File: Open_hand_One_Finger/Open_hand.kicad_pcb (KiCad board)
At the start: 2 copper layers, 21 x 101.6 mm, 28 parts, among them U1 LIS3MDL, U2 MAX32660GTP, U4 ICM-40608, U5 ICM-40608, U6 ICM-40608

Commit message: add swd conector
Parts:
- added C15: 1u, Capacitor_SMD:C_0603_1608Metric, F.Cu at (170.9, 108.7)
- added C16: 1u, Capacitor_SMD:C_0603_1608Metric, F.Cu at (170.9, 110.3)
- added C17: 1u, Capacitor_SMD:C_0603_1608Metric, F.Cu at (189.0, 106.4)
- added J1: Conn_ARM_JTAG_SWD_10, Connector:Tag-Connect_TC2050-IDC-FP_2x05_P1.27mm_Vertical, F.Cu at (184.0, 105.6)
- added Y1: 32.768kHz,6pF, Crystal:Crystal_SMD_3215-2Pin_3.2x1.5mm, F.Cu at (170.7, 105.9)
- moved U2 3.23 mm to (175.1, 107.6), turned to -90 degrees
- moved TP3 1.07 mm to (167.9, 102.9)
- moved TP2 0.76 mm to (165.5, 103.0)
- moved TP4 0.49 mm to (171.7, 102.6)
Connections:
- net /IMU/INT1 renamed /INT0
- net /IMU1/INT1 renamed /INT1
- net /IMU2/INT1 renamed /INT2
- net /MAG/DRDY renamed /DREADY
- U2 pad 10: unconnected-(U2-VCORE-Pad10) -> Net-(U2-VCORE)
- U2 pad 7: unconnected-(U2-32KOUT-Pad7) -> Net-(U2-32KOUT)
- U2 pad 8: unconnected-(U2-32KIN-Pad8) -> Net-(U2-32KIN)
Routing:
- net Net-(U2-32KOUT): track 0.00 -> 4.18 mm
- net Net-(U2-32KIN): track 0.00 -> 2.68 mm
- net Net-(U2-VCORE): track 0.00 -> 2.60 mm
- net +3.3V: track 13.7 -> 15.5 mm
- net GND: track 19.4 -> 20.8 mm, vias 0 -> 2
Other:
- board size 21 x 101.6 mm -> 28.9 x 100 mm
- board text added: "0.0800 mm / 0.0800 mm"
- board text added: "0.1100 mm"
- board text added: "0.2500 mm"
- board text added: "2"
- board text added: "20.9898 mm x 99.9950 mm"
- board text added: "BOARD CHARACTERISTICS"
- board text added: "Board Thickness:"
- board text added: "Board overall dimensions:"
- board text added: "Castellated pads:"
- board text added: "Copper Finish:"
- board text added: "Copper Layer Count:"
- board text added: "Edge card connectors:"
- board text added: "Impedance Control:"
- board text added: "Min hole diameter:"
- board text added: "Min track/spacing:"
- board text added: "No"
- board text added: "None"
- board text added: "Plated Board Edge:"
- board text added: "Yes"

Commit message: making the pcb look less like a dick
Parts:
- added J2: DF37C-24DP-0.4V(51), DF37C-24DP-0.4V(51):DF37C-24DP-0.4V(51), B.Cu at (169.1, 124.5)
- moved TP9 13.4 mm to (167.3, 43.2)
- moved C10 9.67 mm to (171.5, 38.8)
- moved C11 9.67 mm to (173.6, 43.4)
- moved C9 9.67 mm to (171.5, 40.4)
- moved U6 9.67 mm to (171.5, 43.2)
- moved TP8 4.88 mm to (168.1, 65.2)
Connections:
- U1 pad 7: /MAG/INT -> /INT_MAG
- U2 pad 5: unconnected-(U2-~{RSTN}-Pad5) -> /RST
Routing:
- net +3.3V: track 15.5 -> 135.7 mm
- net /CS2: track 0.00 -> 69.3 mm
- net /DIN: track 4.11 -> 69.9 mm
- net /CLK: track 4.26 -> 70.0 mm
- net /DOUT: track 4.70 -> 69.7 mm, vias 4 -> 2
- net /INT2: track 0.00 -> 57.3 mm, vias 0 -> 1
- net /CS1: track 0.00 -> 5.84 mm, vias 0 -> 2
- net GND: track 20.8 -> 16.9 mm, vias 2 -> 10
- net /INT1: track 0.00 -> 1.84 mm
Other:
- board size 28.9 x 100 mm -> 28.9 x 88.2 mm

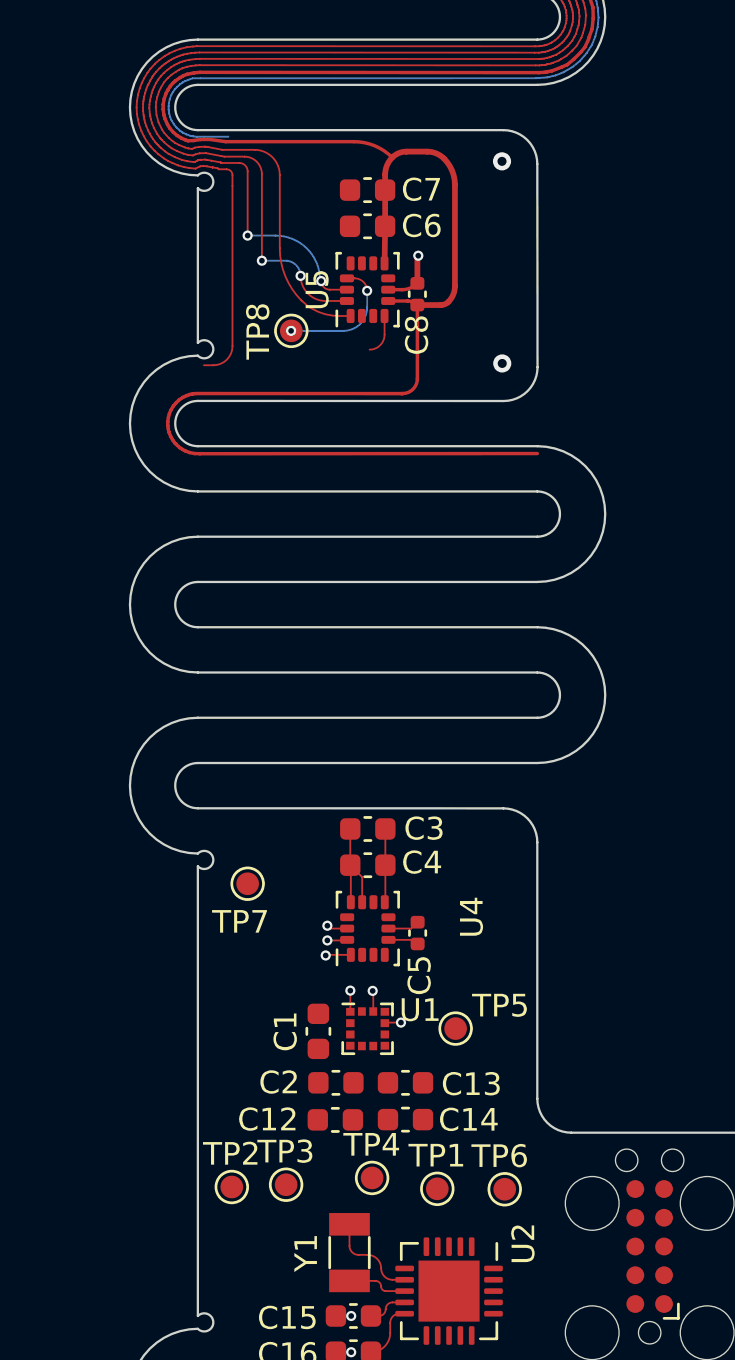
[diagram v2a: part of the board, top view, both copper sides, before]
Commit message: adding coverlay slit so emi shield is connected to gnd more routing
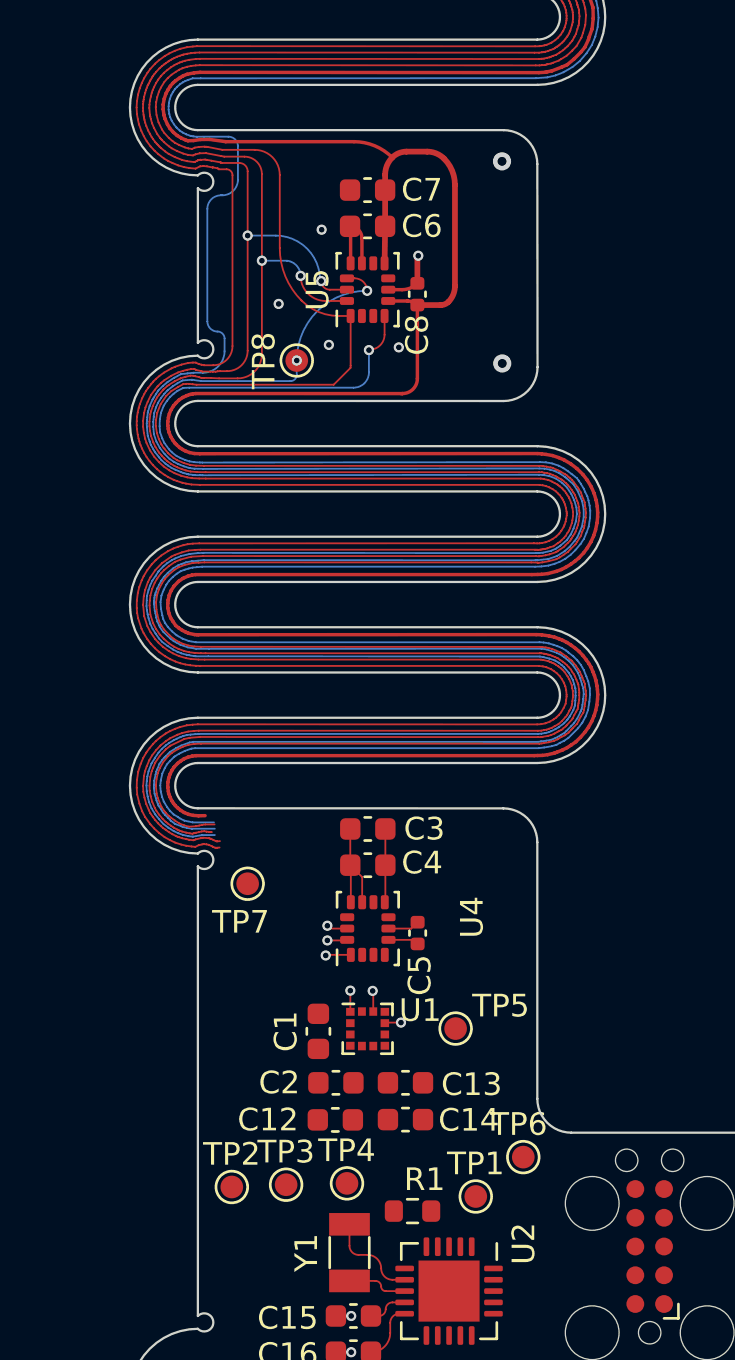
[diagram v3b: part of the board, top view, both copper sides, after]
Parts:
- added R1: R_US, Resistor_SMD:R_0603_1608Metric, F.Cu at (173.5, 104.1)
- moved TP1 1.73 mm to (176.3, 103.4)
- moved TP6 1.64 mm to (178.4, 101.7)
- moved TP8 1.33 mm to (168.4, 66.5)
- moved TP4 1.14 mm to (170.6, 102.8)
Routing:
- net /INT2: track 57.3 -> 162.9 mm
- net /CLK: track 70.0 -> 171.6 mm
- net /DOUT: track 69.7 -> 170.7 mm
- net /DIN: track 69.9 -> 169.9 mm
- net /INT1: track 1.84 -> 101.9 mm, vias 0 -> 1
- net /CS1: track 5.84 -> 103.1 mm
- net /CS2: track 69.3 -> 164.3 mm
- net +3.3V: track 135.7 -> 206.1 mm
- net GND: track 16.9 -> 20.4 mm, vias 10 -> 14

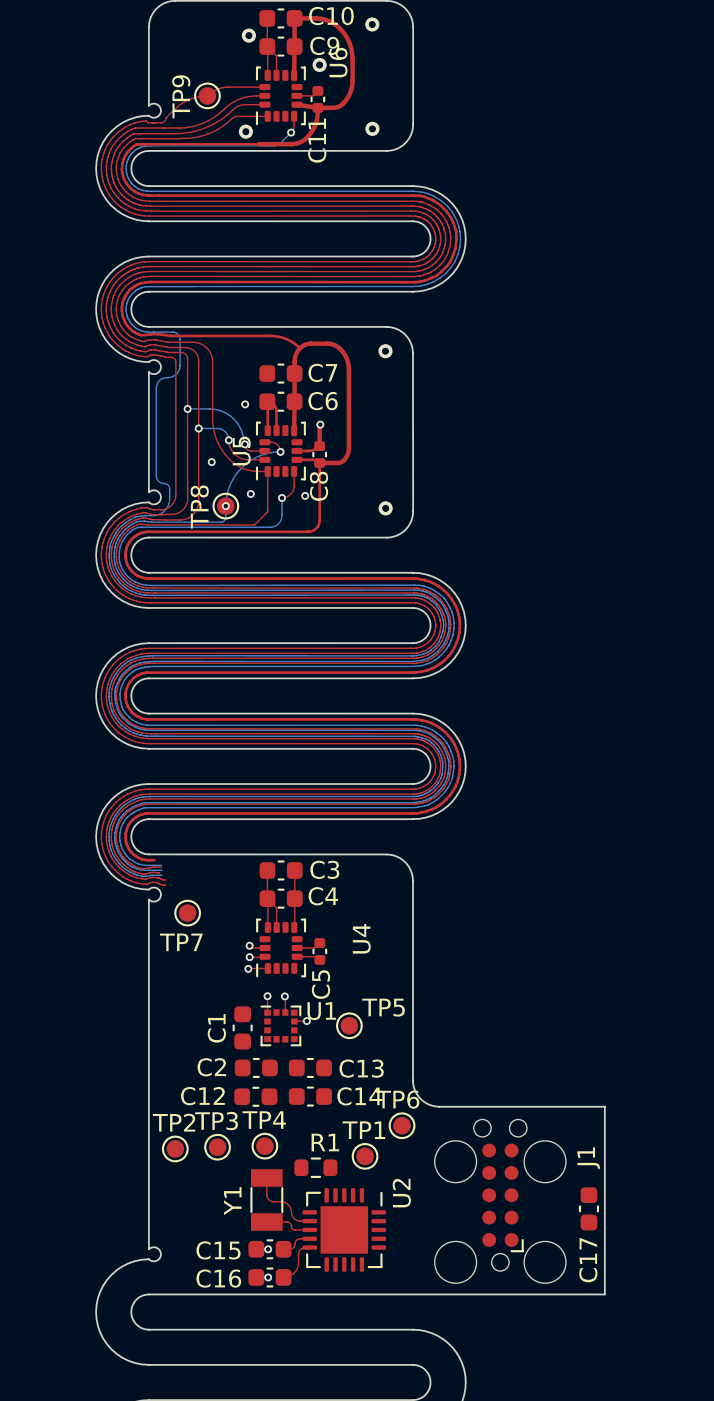
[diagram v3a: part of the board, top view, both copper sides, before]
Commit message: new copper pour rules
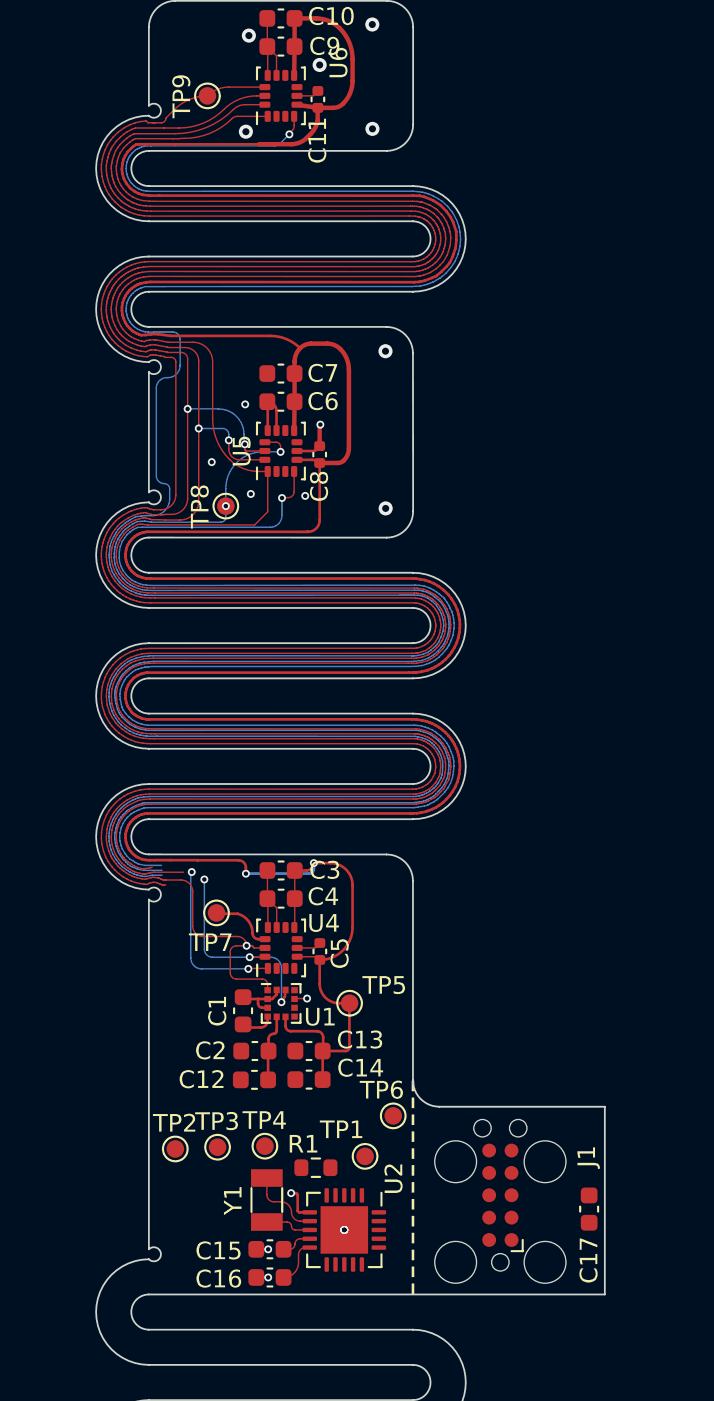
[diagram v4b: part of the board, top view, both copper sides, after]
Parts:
- moved TP7 1.64 mm to (167.8, 89.6)
- moved TP5 1.28 mm to (175.4, 94.7)
- moved U1 1.28 mm to (171.5, 94.7)
- moved C1 0.97 mm to (169.3, 95.2)
- moved C13 0.97 mm to (173.1, 97.4)
- moved C14 0.97 mm to (173.1, 99.1)
- moved C12 0.97 mm to (170.0, 99.1)
- moved C2 0.97 mm to (170.0, 97.4)
- moved TP6 0.75 mm to (177.9, 101.1)
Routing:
- net +3.3V: track 206.1 -> 242.9 mm, vias 0 -> 2
- net /CLK: track 171.6 -> 184.0 mm, vias 4 -> 3
- net /DIN: track 169.9 -> 182.3 mm, vias 4 -> 5
- net /DOUT: track 170.7 -> 178.7 mm, vias 2 -> 3
- net GND: track 20.4 -> 25.8 mm, vias 14 -> 18
- net /CS0: track 0.00 -> 3.59 mm
- net Net-(U1-C1): track 0.00 -> 1.92 mm
- net /CS1: track 103.1 -> 103.7 mm
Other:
- board text added: "28.8949 mm x 88.2250 mm"
- board text removed: "20.9898 mm x 99.9950 mm"

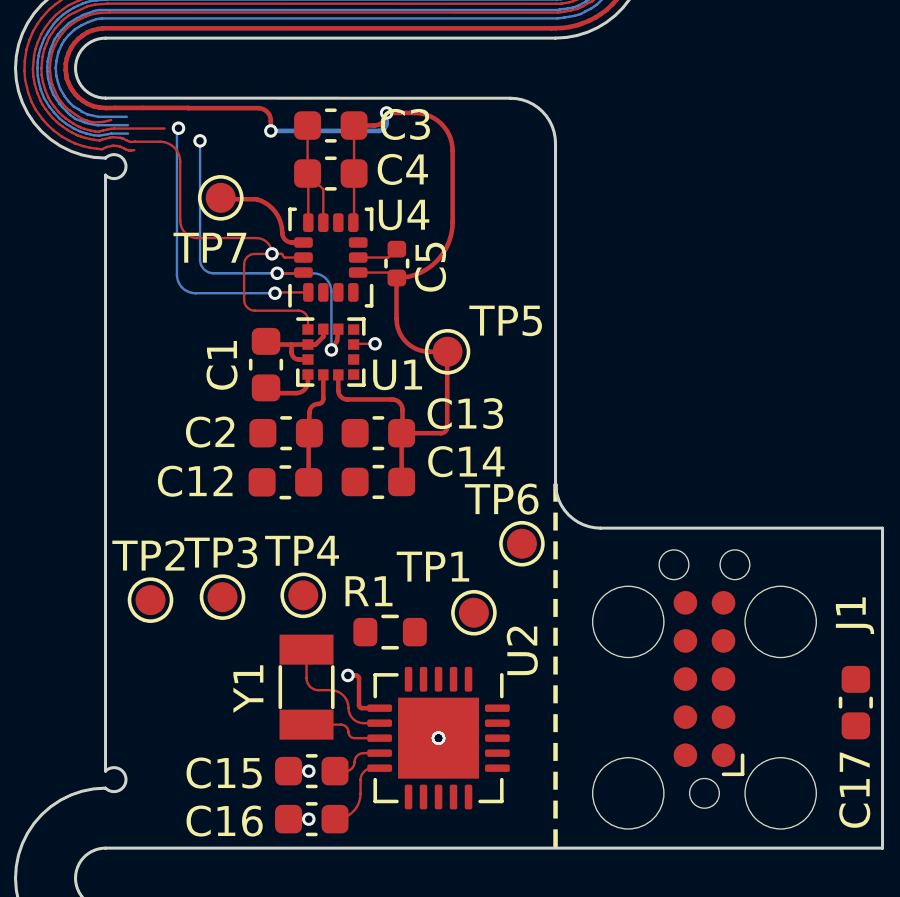
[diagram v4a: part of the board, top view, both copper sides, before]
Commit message: ajout des infos dans la cartouche
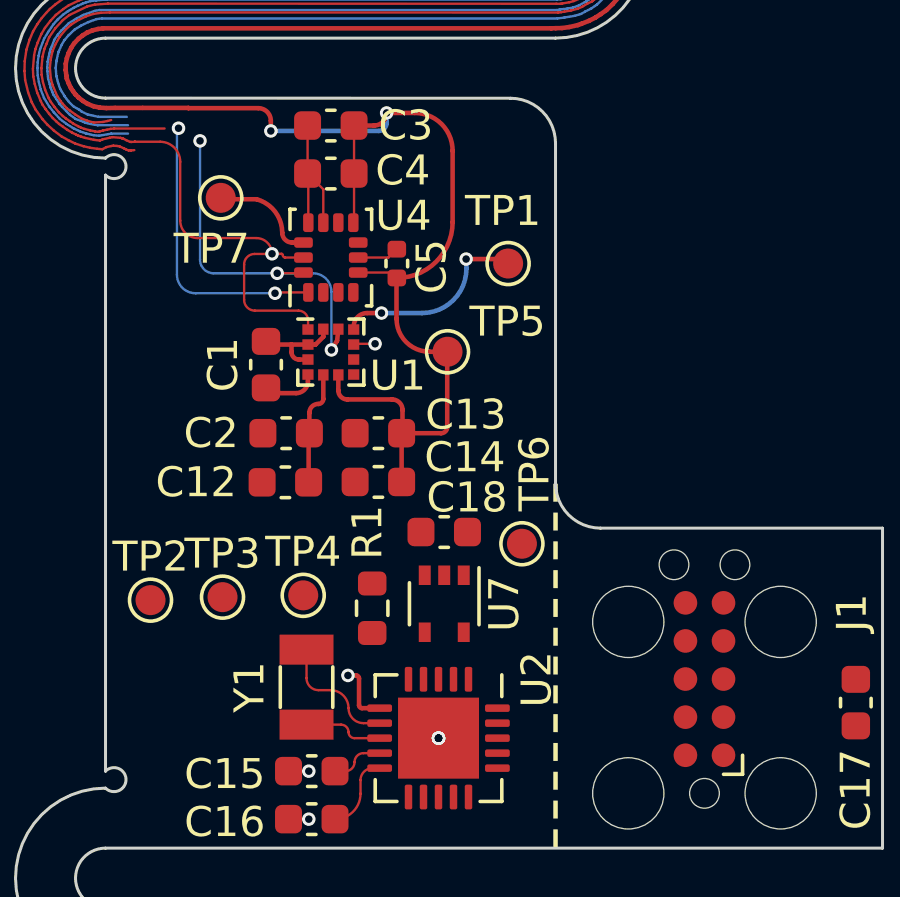
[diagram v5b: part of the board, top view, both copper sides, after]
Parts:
- added C18: 1u, Capacitor_SMD:C_0603_1608Metric, F.Cu at (175.3, 100.7)
- added U7: SN74AHC1G02DCKR, Package_TO_SOT_SMD:SOT-353_SC-70-5, F.Cu at (175.3, 103.1)
- moved TP1 11.7 mm to (177.4, 91.8)
- moved R1 0.99 mm to (172.9, 103.3), turned to -90 degrees
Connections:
- U2 pad 3: unconnected-(U2-P0.13-Pad3) -> Net-(U2-P0.13)
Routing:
- net /CS_MAG: track 0.00 -> 6.69 mm, vias 0 -> 2
